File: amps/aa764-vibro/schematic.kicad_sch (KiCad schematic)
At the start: 49 parts, among them J1 vibrato pedal, T1 125P1B, T2 125A35A

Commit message: Add: real tube pin numbers and readable valve glyphs on every schematic
Phase B of the drawing program. A factory service sheet numbers every tube
pin, because the number is what a technician puts a probe on. This corpus
printed none, and the numbers hidden in its symbols were positional
placeholders (P=1, G=2, K=3) that would have published a 6V6GT's plate as
pin 1 when it is pin 3.

1055 electrodes now carry the real number, 1027 lettered (27 are shared
filaments deduped, 1 dropped for want of clear space on the 6G2). Resolved per
instance from reference/tubes/<slug>.yaml through the same alias resolution the
layout renderer uses, so a 12AX7 section and a 6SL7 section each get their own
basing. A valve whose basing the corpus does not carry prints nothing rather
than a wrong number.

Section letters and basing units are now separate things, which cost a detour
worth recording. The RCA 12AX7-A sheet reads "Pin 1 - Plate of Unit No.2 ...
Pin 6 - Plate of Unit No.1", so unit numbering is not pin order; the 5Y3 and
GZ34 number their units in opposite pin order, so nothing positional can
express it. But the section LETTER is a designator, not a basing fact: this
corpus, like every technician, calls the first stage in signal order V1A, and
five amps' prose already did. On four amps the factory sheets put that first
stage on the other half -- the AA764's own schematic prints +200 V on pin 1 --
so those drawings now state their unit explicitly, each citing its source, and
no letter, netlist, parts list or layout comment changed. 183 layout comments
agree with the printed numbers, 0 disagree. A guard fires if two halves of one
bottle resolve to the same unit, which is exactly how this was found.

Glyphs: the cathode gains a bracket and filament hairpin so it can no longer be
confused with the plate bar, the pentode's screen sits on its own row, and a
rectifier draws as one envelope over its sections instead of two apparent
bottles. Line weights are scaled per sheet to a co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
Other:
- note added: "1"
- note added: "2"
- note added: "2,8"
- note added: "3"
- note added: "4"
- note added: "5"
- note added: "6"
- note added: "7"
- note added: "8"
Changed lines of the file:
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@@
   (wire (pts (xy 45.069 38.278) (xy 45.069 42.278))
     (stroke (width 0) (type default)))
-  (junction (at 45.069 38.278) (diameter 0) (color 0 0 0 0))
+  (junction (at 45.069 38.278) (diameter 1.316) (color 0 0 0 0))
   (symbol (lib_id "cx:R") (at 45.069 46.088 0) (unit 1)
     (in_bom yes) (on_board yes)
@@
   (global_label "GND" (shape input) (at 57.069 54.898 270)
     (effects (font (size 1.27 1.27)) (justify right)))
-  (junction (at 57.069 27.178) (diameter 0) (color 0 0 0 0))
+  (junction (at 57.069 27.178) (diameter 1.316) (color 0 0 0 0))
   (wire (pts (xy 57.069 27.178) (xy 69.069 27.178))
     (stroke (width 0) (type default)))
@@
   (wire (pts (xy 69.069 27.178) (xy 69.069 32.278))
     (stroke (width 0) (type default)))
-  (junction (at 69.069 27.178) (diameter 0) (color 0 0 0 0))
+  (junction (at 69.069 27.178) (diameter 1.316) (color 0 0 0 0))
   (symbol (lib_id "cx:C") (at 81.069 24.658 90) (unit 1)
     (in_bom yes) (on_board yes)
@@
   (wire (pts (xy 78.879 32.278) (xy 83.069 32.278))
     (stroke (width 0) (type default)))
-  (junction (at 83.069 32.278) (diameter 0) (color 0 0 0 0))
+  (junction (at 83.069 32.278) (diameter 1.316) (color 0 0 0 0))
   (symbol (lib_id "cx:C") (at 90.069 32.278 90) (unit 1)
     (in_bom yes) (on_board yes)
@@
     (property "Reference" "VR3" (at 101.469 32.888 0) (effects (font (size 1.27 1.27)) (justify left)))
     (property "Value" "250k bass" (at 101.469 35.288 0) (effects (font (size 1.27 1.27)) (justify left))))
-  (junction (at 97.069 32.278) (diameter 0) (color 0 0 0 0))
+  (junction (at 97.069 32.278) (diameter 1.316) (color 0 0 0 0))
   (wire (pts (xy 102.149 36.088) (xy 105.069 36.088))
     (stroke (width 0) (type default)))
@@
   (wire (pts (xy 135.069 63.898) (xy 143.069 63.898))
     (stroke (width 0) (type default)))
-  (junction (at 135.069 63.898) (diameter 0) (color 0 0 0 0))
+  (junction (at 135.069 63.898) (diameter 1.316) (color 0 0 0 0))
   (symbol (lib_id "cx:R") (at 135.069 67.708 0) (unit 1)
     (in_bom yes) (on_board yes)
@@
   (global_label "SPKR" (shape input) (at 123.069 71.518 270)
     (effects (font (size 1.27 1.27)) (justify right)))
-  (junction (at 135.069 35.178) (diameter 0) (color 0 0 0 0))
+  (junction (at 135.069 35.178) (diameter 1.316) (color 0 0 0 0))
   (wire (pts (xy 135.069 35.178) (xy 143.069 35.178))
     (stroke (width 0) (type default)))
@@
   (wire (pts (xy 161.069 35.178) (xy 161.069 46.278))
     (stroke (width 0) (type default)))
-  (junction (at 161.069 46.278) (diameter 0) (color 0 0 0 0))
+  (junction (at 161.069 46.278) (diameter 1.316) (color 0 0 0 0))
   (symbol (lib_id "cx:R") (at 161.069 50.088 0) (unit 1)
     (in_bom yes) (on_board yes)
@@
   (global_label "GND" (shape input) (at 175.069 63.898 270)
     (effects (font (size 1.27 1.27)) (justify right)))
-  (junction (at 175.069 56.278) (diameter 0) (color 0 0 0 0))
+  (junction (at 175.069 56.278) (diameter 1.316) (color 0 0 0 0))
   (wire (pts (xy 175.069 56.278) (xy 182.689 56.278))
     (stroke (width 0) (type default)))
@@
   (wire (pts (xy 13.989 189.738) (xy 31.069 189.738))
     (stroke (width 0) (type default)))
-  (junction (at 31.069 189.738) (diameter 0) (color 0 0 0 0))
+  (junction (at 31.069 189.738) (diameter 1.316) (color 0 0 0 0))
   (symbol (lib_id "cx:R") (at 31.069 193.548 0) (unit 1)
     (in_bom yes) (on_board yes)
@@
   (wire (pts (xy 49.069 196.278) (xy 51.449 196.278))
     (stroke (width 0) (type default)))
-  (junction (at 49.069 196.278) (diameter 0) (color 0 0 0 0))
+  (junction (at 49.069 196.278) (diameter 1.316) (color 0 0 0 0))
   (symbol (lib_id "cx:R") (at 49.069 200.088 0) (unit 1)
     (in_bom yes) (on_board yes)
@@
   (global_label "GND" (shape input) (at 59.069 214.898 270)
     (effects (font (size 1.27 1.27)) (justify right)))
-  (junction (at 59.069 185.178) (diameter 0) (color 0 0 0 0))
+  (junction (at 59.069 185.178) (diameter 1.316) (color 0 0 0 0))
   (symbol (lib_id "cx:C") (at 71.069 185.178 90) (unit 1)
     (in_bom yes) (on_board yes)
@@
   (wire (pts (xy 107.069 203.898) (xy 107.069 207.278))
     (stroke (width 0) (type default)))
-  (junction (at 107.069 207.278) (diameter 0) (color 0 0 0 0))
+  (junction (at 107.069 207.278) (diameter 1.316) (color 0 0 0 0))
   (symbol (lib_id "cx:R") (at 107.069 211.088 0) (unit 1)
     (in_bom yes) (on_board yes)
@@
   (symbol (lib_id "cx:DIODE_TUBE") (at 81.069 124.398 0) (unit 1)
     (in_bom yes) (on_board yes)
-    (property "Reference" "V3A" (at 69.3448 124.678 0) (effects (font (size 1.27 1.27)) (justify left)))
-    (property "Value" "5Y3GT" (at 69.3448 127.078 0) (effects (font (size 1.27 1.27)) (justify left))))
+    (property "Reference" "V3A" (at 78.275 131.278 0) (effects (font (size 1.27 1.27)) (justify left)))
+    (property "Value" "5Y3GT" (at 78.275 133.678 0) (effects (font (size 1.27 1.27)) (justify left))))
   (global_label "HT_B" (shape input) (at 93.069 114.278 90)
     (effects (font (size 1.27 1.27)) (justify left)))
@@
   (wire (pts (xy 99.069 134.278) (xy 107.069 134.278))
     (stroke (width 0) (type default)))
-  (junction (at 93.069 134.278) (diameter 0) (color 0 0 0 0))
-  (junction (at 99.069 134.278) (diameter 0) (color 0 0 0 0))
+  (junction (at 93.069 134.278) (diameter 1.316) (color 0 0 0 0))
+  (junction (at 99.069 134.278) (diameter 1.316) (color 0 0 0 0))
   (symbol (lib_id "cx:C") (at 99.069 138.088 0) (unit 1)
     (in_bom yes) (on_board yes)
@@
   (wire (pts (xy 127.069 134.278) (xy 129.069 134.278))
     (stroke (width 0) (type default)))
-  (junction (at 123.069 134.278) (diameter 0) (color 0 0 0 0))
+  (junction (at 123.069 134.278) (diameter 1.316) (color 0 0 0 0))
   (global_label "B+2" (shape input) (at 123.069 129.278 90)
     (effects (font (size 1.27 1.27)) (justify left)))
   (wire (pts (xy 123.069 129.278) (xy 123.069 134.278))
     (stroke (width 0) (type default)))
-  (junction (at 127.069 134.278) (diameter 0) (color 0 0 0 0))
+  (junction (at 127.069 134.278) (diameter 1.316) (color 0 0 0 0))
   (symbol (lib_id "cx:C") (at 127.069 138.088 0) (unit 1)
     (in_bom yes) (on_board yes)
@@
   (wire (pts (xy 143.069 134.278) (xy 149.069 134.278))
     (stroke (width 0) (type default)))
-  (junction (at 143.069 134.278) (diameter 0) (color 0 0 0 0))
+  (junction (at 143.069 134.278) (diameter 1.316) (color 0 0 0 0))
   (global_label "B+3" (shape input) (at 143.069 129.278 90)
     (effects (font (size 1.27 1.27)) (justify left)))
@@
   (global_label "GND" (shape input) (at 187.069 121.278 270)
     (effects (font (size 1.27 1.27)) (justify right)))
+  (polyline (pts (xy 93.069 119.318) (xy 94.06 119.416) (xy 95.013 119.705) (xy 95.891 120.174) (xy 96.661 120.806) (xy 97.293 121.576) (xy 97.762 122.454) (xy 98.051 123.407) (xy 98.149 124.398) (xy 98.051 125.389) (xy 97.762 126.342) (xy 97.293 127.22) (xy 96.661 127.99) (xy 95.891 128.622) (xy 95.013 129.091) (xy 94.06 129.38) (xy 93.069 129.478) (xy 81.069 129.478) (xy 80.078 129.38) (xy 79.125 129.091) (xy 78.247 128.622) (xy 77.477 127.99) (xy 76.845 127.22) (xy 76.376 126.342) (xy 76.087 125.389) (xy 75.989 124.398) (xy 76.087 123.407) (xy 76.376 122.454) (xy 76.845 121.576) (xy 77.477 120.806) (xy 78.247 120.174) (xy 79.125 119.705) (xy 80.078 119.416) (xy 81.069 119.318) (xy 93.069 119.318))
+    (stroke (width 0.445) (type default) (color 197 163 255 1)) (fill (type none)))
+  (polyline (pts (xy 79.169 126.633) (xy 81.069 125.033) (xy 87.069 127.113) (xy 93.069 125.033) (xy 94.969 126.633))
+    (stroke (width 0.445) (type default) (color 197 163 255 1)) (fill (type none)))
+  (text "1" (at 57.919 31.928 0)
+    (effects (font (size 1.1 1.1)) (justify left)))
+  (text "2" (at 50.1218 36.878 0)
+    (effects (font (size 1.1 1.1)) (justify left)))
+  (text "3" (at 57.919 44.628 0)
+    (effects (font (size 1.1 1.1)) (justify left)))
+  (text "6" (at 135.919 39.928 0)
+    (effects (font (size 1.1 1.1)) (justify left)))
+  (text "7" (at 128.122 44.878 0)
+    (effects (font (size 1.1 1.1)) (justify left)))
+  (text "8" (at 135.919 52.628 0)
+    (effects (font (size 1.1 1.1)) (justify left)))
+  (text "3" (at 175.919 39.293 0)
+    (effects (font (size 1.1 1.1)) (justify left)))
+  (text "5" (at 168.122 44.878 0)
+    (effects (font (size 1.1 1.1)) (justify left)))
+  (text "4" (at 180.969 43.608 0)
+    (effects (font (size 1.1 1.1)) (justify left)))
+  (text "8" (at 175.919 51.993 0)
+    (effects (font (size 1.1 1.1)) (justify left)))
+  (text "6" (at 59.919 189.928 0)
+    (effects (font (size 1.1 1.1)) (justify left)))
+  (text "7" (at 52.1218 194.878 0)
+    (effects (font (size 1.1 1.1)) (justify left)))
+  (text "8" (at 59.919 202.628 0)
+    (effects (font (size 1.1 1.1)) (justify left)))
+  (text "1" (at 107.919 189.928 0)
+    (effects (font (size 1.1 1.1)) (justify left)))
+  (text "2" (at 100.122 194.878 0)
+    (effects (font (size 1.1 1.1)) (justify left)))
+  (text "3" (at 107.919 202.628 0)
+    (effects (font (size 1.1 1.1)) (justify left)))
+  (text "6" (at 81.919 118.048 0)
+    (effects (font (size 1.1 1.1)) (justify left)))
+  (text "2,8" (at 81.919 130.748 0)
+    (effects (font (size 1.1 1.1)) (justify left)))
+  (text "4" (at 93.919 118.048 0)
+    (effects (font (size 1.1 1.1)) (justify left)))
   (text "Heaters (6.3 V, one leg grounded), pilot lamp, AC switch and fuse omitted here — see netlist.cir, notes.md, layout.yaml. Rails: B+1 +355 · B+2 +340 screen · B+3 +320 preamp. Audio path is component-for-component amps/aa764" (at 12.7 235.056 0)
     (effects (font (size 1.2 1.2)) (justify left)))

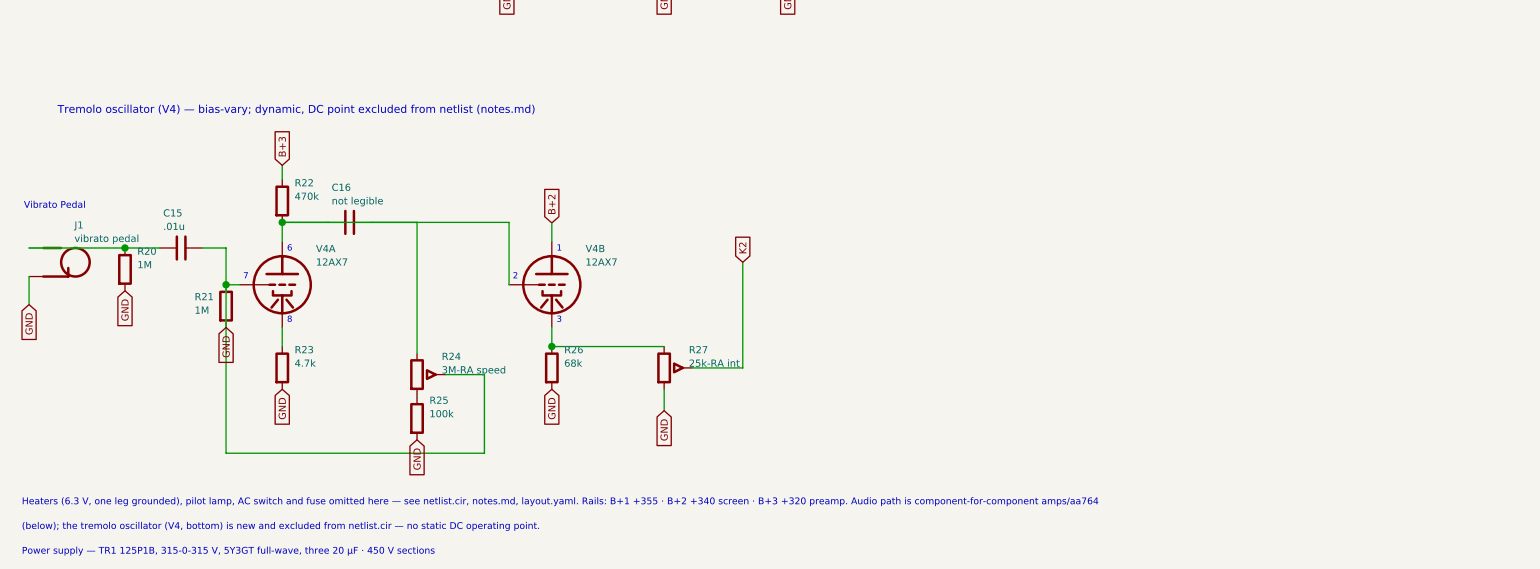
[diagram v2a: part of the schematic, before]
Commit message: Fix: schematic sheet notes no longer name repository files
Thirty-seven committed sheets rendered footnotes and section notes such as
"Heaters and PT primary omitted — see netlist.cir and meta.yaml" or
"excluded from netlist.cir (notes.md)" to visitors through KiCanvas. The
prose sweeps never counted sheets. Rewritten in the site's own words — the
netlist, the sources list, the circuit story, the parts list, the board
drawing — in 59 strings across 33 draw scripts, keeping every technical
claim as it was; the three tone sheets (6G4, 6G5, 6G6-B) are under repair
elsewhere and keep theirs for now. The sweep touched only strings passed to
the sheet's note, text, caption and footnote calls, never a path or a value.

Gates: check_schematics 40/0, connectivity 0 isolated pins;
verify_schematic_nets 40 clean; only the regenerated sheets and their served
copies changed.

Co-Authored-By: Claude Fable 5.1 <noreply@anthropic.com>
Claude-Session: https://claude.ai/code/session_01KBMfdh37HmCL2iWcBiL5J1
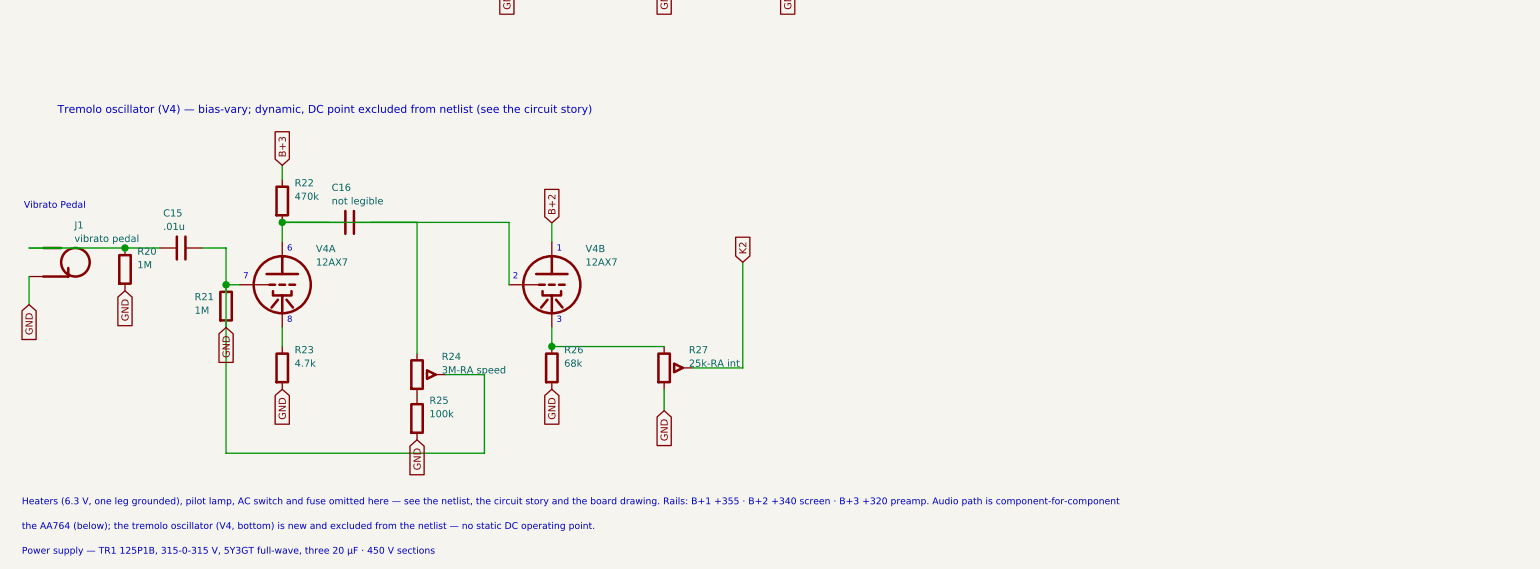
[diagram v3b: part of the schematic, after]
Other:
- note added: "Heaters (6.3 V, one leg grounded), pilot lamp, AC switch and fuse omitted here — see the netlist, the circuit story and the board drawing. Rails: B+1 +355 · B+2 +340 screen · B+3 +320 preamp. Audio path is component-for-component"
- note added: "Tremolo oscillator (V4) — bias-vary; dynamic, DC point excluded from netlist (see the circuit story)"
- note added: "the AA764 (below); the tremolo oscillator (V4, bottom) is new and excluded from the netlist — no static DC operating point."
- note removed: "(below); the tremolo oscillator (V4, bottom) is new and excluded from netlist.cir — no static DC operating point."
- note removed: "Heaters (6.3 V, one leg grounded), pilot lamp, AC switch and fuse omitted here — see netlist.cir, notes.md, layout.yaml. Rails: B+1 +355 · B+2 +340 screen · B+3 +320 preamp. Audio path is component-for-component amps/aa764"
- note removed: "Tremolo oscillator (V4) — bias-vary; dynamic, DC point excluded from netlist (notes.md)"
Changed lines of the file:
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@@
 (kicad_sch (version 20231120) (generator "circuit-codex")
-  (paper "User" 237.95 280.70)
+  (paper "User" 241.82 280.70)
   (title_block
     (title "AA764 (Vibro) — Blackface Vibro Champ-style")
@@
   (global_label "GND" (shape input) (at 220.069 37.358 0)
     (effects (font (size 1.27 1.27)) (justify left)))
-  (text "Tremolo oscillator (V4) — bias-vary; dynamic, DC point excluded from netlist (notes.md)" (at 19.069 165.278 0)
+  (text "Tremolo oscillator (V4) — bias-vary; dynamic, DC point excluded from netlist (see the circuit story)" (at 19.069 165.278 0)
     (effects (font (size 1.4 1.4)) (justify left)))
   (symbol (lib_id "cx:JACK") (at 19.069 192.278 0) (unit 1)
@@
   (text "4" (at 93.919 118.048 0)
     (effects (font (size 1.1 1.1)) (justify left)))
-  (text "Heaters (6.3 V, one leg grounded), pilot lamp, AC switch and fuse omitted here — see netlist.cir, notes.md, layout.yaml. Rails: B+1 +355 · B+2 +340 screen · B+3 +320 preamp. Audio path is component-for-component amps/aa764" (at 12.7 235.056 0)
+  (text "Heaters (6.3 V, one leg grounded), pilot lamp, AC switch and fuse omitted here — see the netlist, the circuit story and the board drawing. Rails: B+1 +355 · B+2 +340 screen · B+3 +320 preamp. Audio path is component-for-component" (at 12.7 235.056 0)
     (effects (font (size 1.2 1.2)) (justify left)))
-  (text "(below); the tremolo oscillator (V4, bottom) is new and excluded from netlist.cir — no static DC operating point." (at 12.7 239.456 0)
+  (text "the AA764 (below); the tremolo oscillator (V4, bottom) is new and excluded from the netlist — no static DC operating point." (at 12.7 239.456 0)
     (effects (font (size 1.2 1.2)) (justify left)))
   (text "Power supply — TR1 125P1B, 315-0-315 V, 5Y3GT full-wave, three 20 µF · 450 V sections" (at 12.7 243.856 0)

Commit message: Add: sheet<->board net-equivalence gate over every part, no netlist (survey + drift-gated worklist)
pipeline/verify_sheet_vs_board.py proves the schematic and the board layout
draw the SAME circuit over the ~1,280 BOM passives the DC netlist does not
model — the parts both existing equivalence gates skip by construction. The
two drawings are authored independently, so their net partitions are each
other's witness: <GND>, tube pins (through basing + the datasheet unit the
sheet states), pot wipers, jack contacts (cx:JACK T/S <-> J.tip/J.sleeve)
and declared net_map.leads anchor the partitions to each other; two-terminal
parts and pot ends resolve as unordered pairs by majority voting; a
section<->unit swap is searched for on every dual-section socket and
reported once. Heaters and the pilot lamp are excluded (check_heaters owns
them); every symbol class the board cannot name is listed in scope.

Declarations (docs/layout-schema.md): a sheet part the board neither places
nor wires must be covered by net_map.netlist_unplaced / series_bridge
(layout or sch_map — a bridged part the board does not place is compared
as one net, the conductor runs through it), a new per-part
net_map.not_on_board, or a new board-scope rule scope.not_drawn
(glob + why). A declaration covering nothing is a STALE DECLARATION.
No amp declares anything yet: that is a source-read job.

schematic_lib: a draw script that states `unit=` now emits it as a hidden
symbol property, Basing_unit, so the gate reads the unit off the sheet and
not the script (the script is the fallback, and the scope line says so).
Sheets drawn without unit= are byte-identical. NOT regenerated here: the
four sheets that state a unit (5e4a, 5f6, aa764, aa764-vibro) need
`draw_<id>.py` + sync-assets before the schematic-drift step of CI passes.

Found at HEAD 07dea48 (reference/sheet-board.yaml, --export), 40 amps,
38 with findings, 36 of them with both drawings claiming verified:
  SECTION-SWAP 25 sockets on 16 sheets, SPLIT 4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
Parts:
- V1A: Basing_unit (none) -> 2
- V1B: Basing_unit (none) -> 1
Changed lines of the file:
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@@
     (in_bom yes) (on_board yes)
     (property "Reference" "V1A" (at 63.069 31.878 0) (effects (font (size 1.27 1.27)) (justify left)))
-    (property "Value" "12AX7" (at 63.069 34.278 0) (effects (font (size 1.27 1.27)) (justify left))))
+    (property "Value" "12AX7" (at 63.069 34.278 0) (effects (font (size 1.27 1.27)) (justify left)))
+    (property "Basing_unit" "2" (at 63.069 36.678 0) (effects (font (size 1.27 1.27)) hide)))
   (wire (pts (xy 45.069 38.278) (xy 49.449 38.278))
     (stroke (width 0) (type default)))
@@
     (in_bom yes) (on_board yes)
     (property "Reference" "V1B" (at 141.069 39.878 0) (effects (font (size 1.27 1.27)) (justify left)))
-    (property "Value" "12AX7" (at 141.069 42.278 0) (effects (font (size 1.27 1.27)) (justify left))))
+    (property "Value" "12AX7" (at 141.069 42.278 0) (effects (font (size 1.27 1.27)) (justify left)))
+    (property "Basing_unit" "1" (at 141.069 44.678 0) (effects (font (size 1.27 1.27)) hide)))
   (wire (pts (xy 121.149 32.278) (xy 124.069 32.278))
     (stroke (width 0) (type default)))
